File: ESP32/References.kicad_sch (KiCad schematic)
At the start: 0 parts

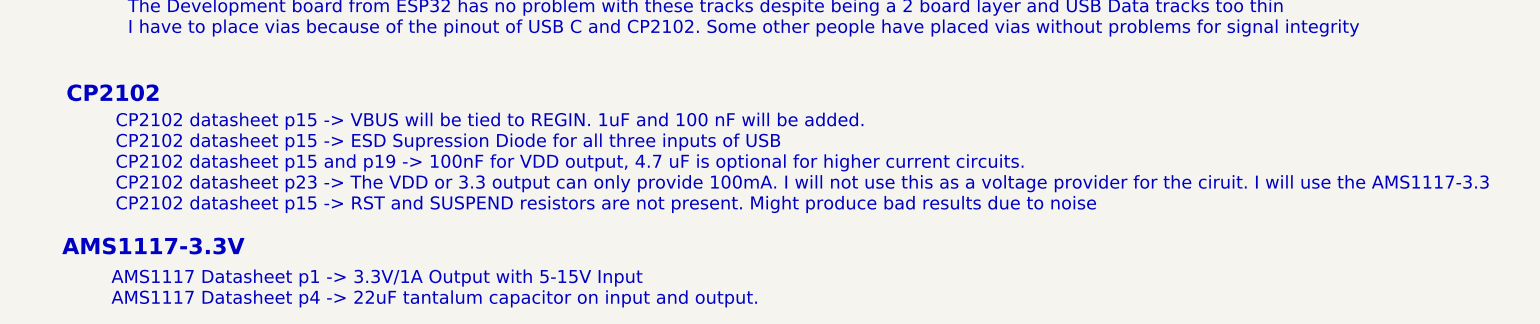
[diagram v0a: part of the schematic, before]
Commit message: ESP32 CP2102 bugfix
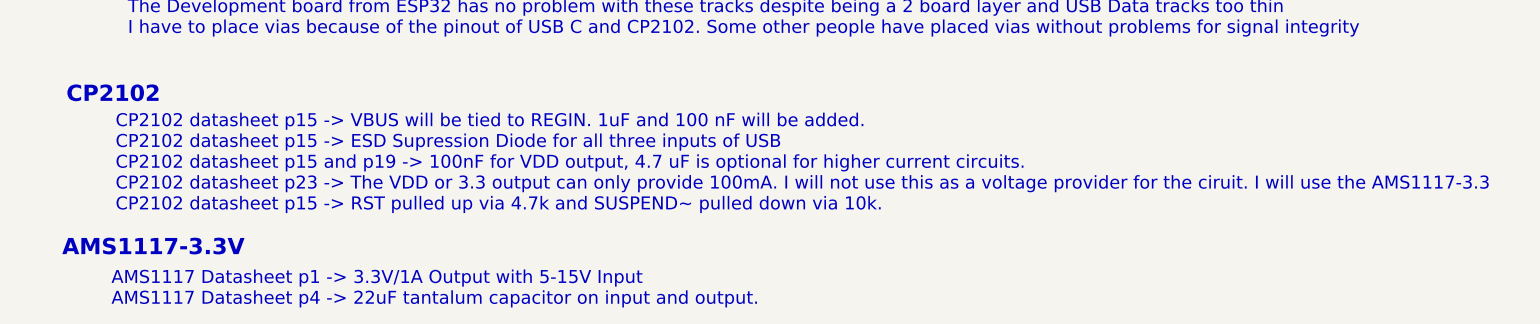
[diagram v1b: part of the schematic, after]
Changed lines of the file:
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@@
 		)
 	)
-	(text "CP2102 datasheet p15 -> VBUS will be tied to REGIN. 1uF and 100 nF will be added.\nCP2102 datasheet p15 -> ESD Supression Diode for all three inputs of USB  \nCP2102 datasheet p15 and p19 -> 100nF for VDD output, 4.7 uF is optional for higher current circuits.\nCP2102 datasheet p23 -> The VDD or 3.3 output can only provide 100mA. I will not use this as a voltage provider for the ciruit. I will use the AMS1117-3.3 \nCP2102 datasheet p15 -> RST and SUSPEND resistors are not present. Might produce bad results due to noise"
+	(text "CP2102 datasheet p15 -> VBUS will be tied to REGIN. 1uF and 100 nF will be added.\nCP2102 datasheet p15 -> ESD Supression Diode for all three inputs of USB  \nCP2102 datasheet p15 and p19 -> 100nF for VDD output, 4.7 uF is optional for higher current circuits.\nCP2102 datasheet p23 -> The VDD or 3.3 output can only provide 100mA. I will not use this as a voltage provider for the ciruit. I will use the AMS1117-3.3 \nCP2102 datasheet p15 -> RST pulled up via 4.7k and SUSPEND~ pulled down via 10k."
 		(exclude_from_sim no)
 		(at 37.465 161.29 0)
